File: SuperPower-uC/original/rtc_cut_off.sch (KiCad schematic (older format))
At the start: 8 parts, among them J601 Conn_01x02_Male, U601 RV-3028-C7

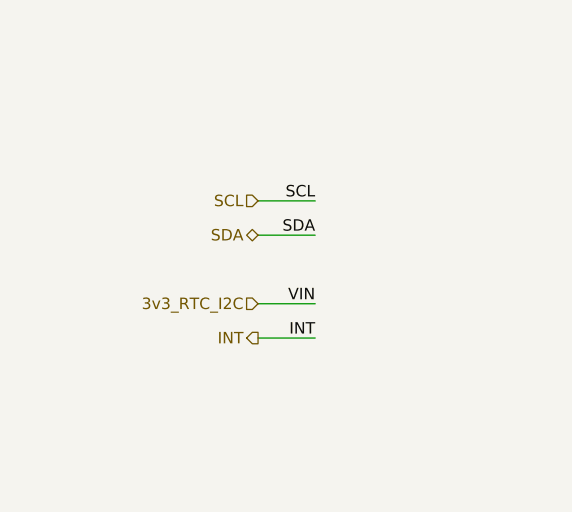
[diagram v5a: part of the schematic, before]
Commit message: Cleanup of text, boxes, label rotations etc. + add labels to main sheet for better overview
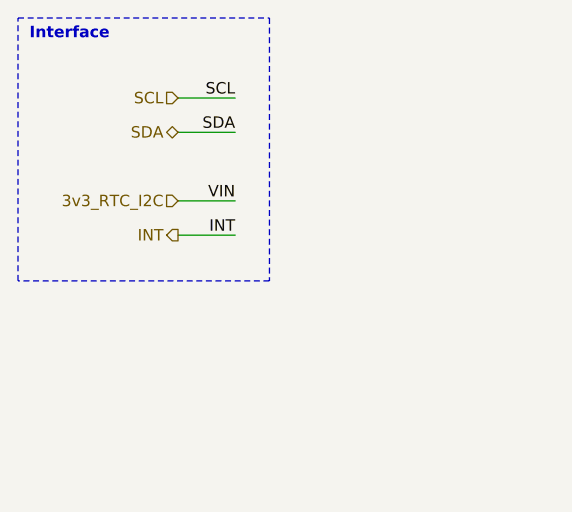
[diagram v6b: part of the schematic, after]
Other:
- note added: "Interface"
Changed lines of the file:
@@
 Comment4 ""
 $EndDescr
-Text HLabel 1600 1350 0    50   Input ~ 0
-SCL
-Text HLabel 1600 1500 0    50   BiDi ~ 0
-SDA
-Text HLabel 1600 1950 0    50   Output ~ 0
+Text HLabel 1250 900  0    50   Input ~ 0
+SCL
+Text HLabel 1250 1050 0    50   BiDi ~ 0
+SDA
+Text HLabel 1250 1500 0    50   Output ~ 0
 INT
 NoConn ~ 5900 3550
@@
 Text Label 4250 3650 0    50   ~ 0
 SDA
-Text Label 1850 1350 2    50   ~ 0
-SCL
-Text Label 1850 1500 2    50   ~ 0
-SDA
-Text Label 1850 1950 2    50   ~ 0
+Text Label 1500 900  2    50   ~ 0
+SCL
+Text Label 1500 1050 2    50   ~ 0
+SDA
+Text Label 1500 1500 2    50   ~ 0
 INT
 Wire Wire Line
-	1600 1950 1850 1950
-Wire Wire Line
-	1600 1350 1850 1350
-Wire Wire Line
-	1600 1500 1850 1500
+	1250 1500 1500 1500
+Wire Wire Line
+	1250 900  1500 900
+Wire Wire Line
+	1250 1050 1500 1050
 Wire Wire Line
 	4500 3550 4250 3550
@@
 Text Label 1650 3850 0    50   ~ 0
 SCL
-Text HLabel 1600 1800 0    50   Input ~ 0
+Text HLabel 1250 1350 0    50   Input ~ 0
 3v3_RTC_I2C
 Text Label 6850 2650 3    50   ~ 0
@@
 VIN
 Wire Wire Line
-	1600 1800 1850 1800
-Text Label 1850 1800 2    50   ~ 0
+	1250 1350 1500 1350
+Text Label 1500 1350 2    50   ~ 0
 VIN
 Wire Wire Line
@@
 Wire Wire Line
 	1650 3200 1650 3450
+Text Notes 600  650  0    50   ~ 10
+Interface
+Wire Notes Line
+	550  550  1650 550
+Wire Notes Line
+	1650 550  1650 1700
+Wire Notes Line
+	1650 1700 550  1700
+Wire Notes Line
+	550  1700 550  550
 $EndSCHEMATC

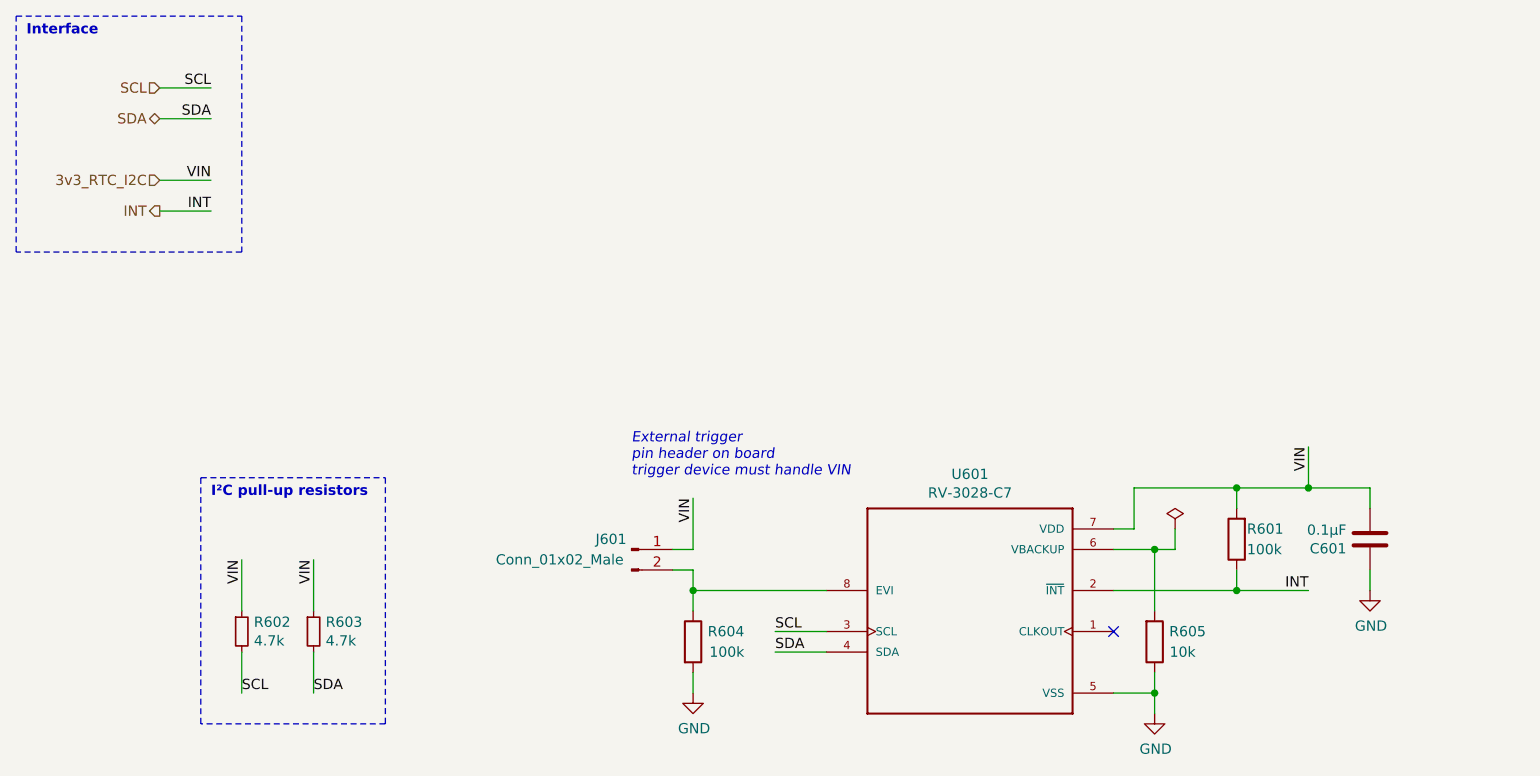
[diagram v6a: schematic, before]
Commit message: Update regulator symbol, changed MOSFET switching of regulators
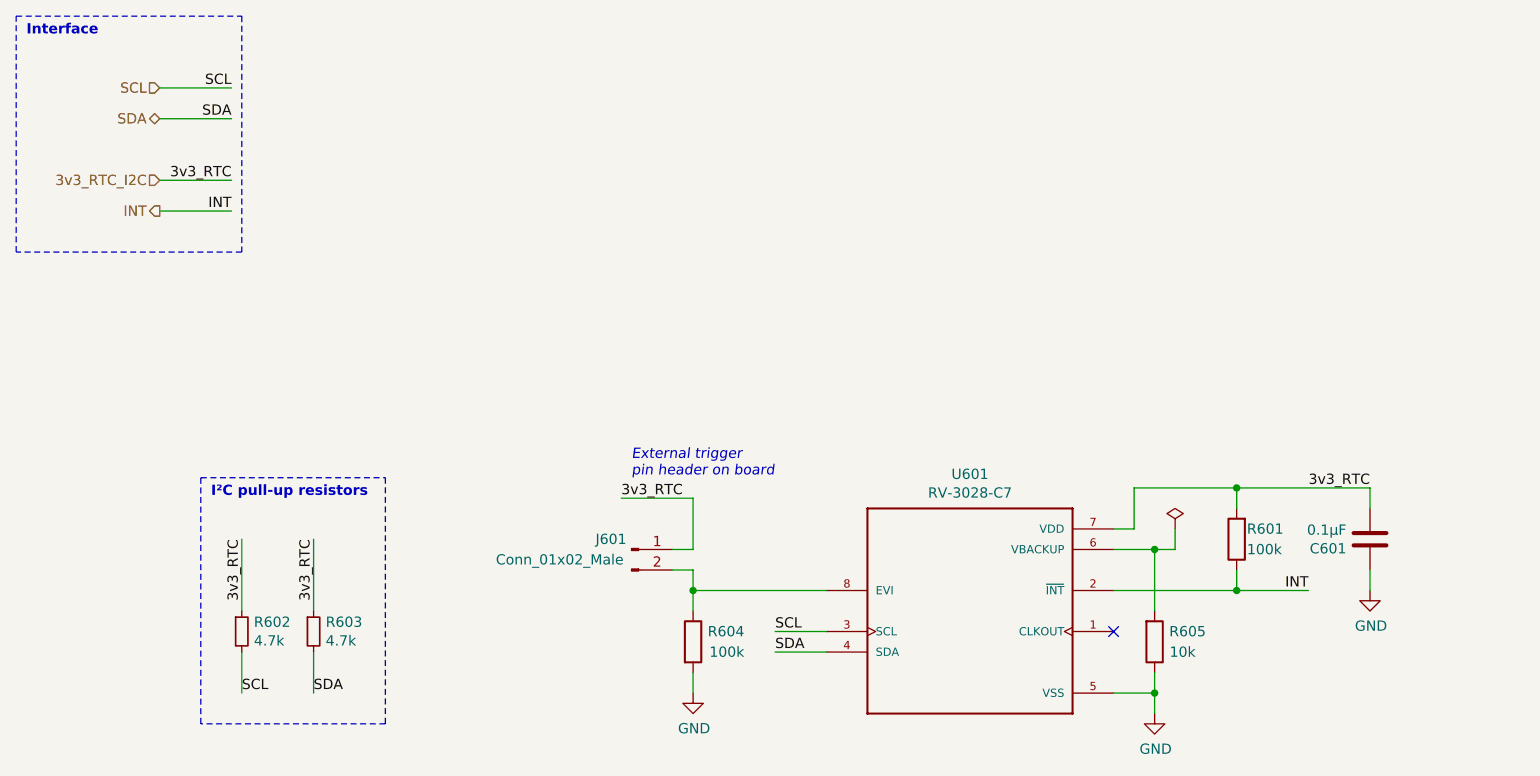
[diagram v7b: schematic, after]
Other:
- note added: "External trigger\npin header on board"
- note removed: "External trigger\npin header on board\ntrigger device must handle VIN"
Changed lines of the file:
@@
 Text Label 4250 3650 0    50   ~ 0
 SDA
-Text Label 1500 900  2    50   ~ 0
+Text Label 1600 900  2    50   ~ 0
 SCL
-Text Label 1500 1050 2    50   ~ 0
+Text Label 1600 1050 2    50   ~ 0
 SDA
-Text Label 1500 1500 2    50   ~ 0
+Text Label 1600 1500 2    50   ~ 0
 INT
 Wire Wire Line
-	1250 1500 1500 1500
-Wire Wire Line
-	1250 900  1500 900
-Wire Wire Line
-	1250 1050 1500 1050
+	1250 1500 1600 1500
+Wire Wire Line
+	1250 900  1600 900
+Wire Wire Line
+	1250 1050 1600 1050
 Wire Wire Line
 	4500 3550 4250 3550
@@
 Wire Wire Line
 	6500 3350 6850 3350
-Wire Wire Line
-	6850 2850 7150 2850
-Wire Wire Line
-	6500 2850 6850 2850
-Connection ~ 6850 2850
 $Comp
 L Device:R_Small R?
@@
 Text HLabel 1250 1350 0    50   Input ~ 0
 3v3_RTC_I2C
-Text Label 6850 2650 3    50   ~ 0
-VIN
-Wire Wire Line
-	6850 2650 6850 2850
+Text Label 7150 2850 2    50   ~ 0
+3v3_RTC
 Wire Wire Line
 	3850 2900 3850 3150
-Text Label 3850 2900 3    50   ~ 0
-VIN
+Text Label 3500 2900 0    50   ~ 0
+3v3_RTC
 Text Notes 3550 2800 0    50   Italic 0
-External trigger\npin header on board\ntrigger device must handle VIN
-Text Label 2000 3200 3    50   ~ 0
-VIN
-Text Label 1650 3200 3    50   ~ 0
-VIN
-Wire Wire Line
-	1250 1350 1500 1350
-Text Label 1500 1350 2    50   ~ 0
-VIN
-Wire Wire Line
-	2000 3200 2000 3450
-Wire Wire Line
-	1650 3200 1650 3450
+External trigger\npin header on board
+Text Label 2000 3100 3    50   ~ 0
+3v3_RTC
+Text Label 1650 3100 3    50   ~ 0
+3v3_RTC
+Wire Wire Line
+	1250 1350 1600 1350
+Text Label 1600 1350 2    50   ~ 0
+3v3_RTC
+Wire Wire Line
+	2000 3100 2000 3450
+Wire Wire Line
+	1650 3100 1650 3450
 Text Notes 600  650  0    50   ~ 10
 Interface
@@
 Wire Notes Line
 	550  1700 550  550
+Wire Wire Line
+	3500 2900 3850 2900
+Wire Wire Line
+	6500 2850 7150 2850
 $EndSCHEMATC

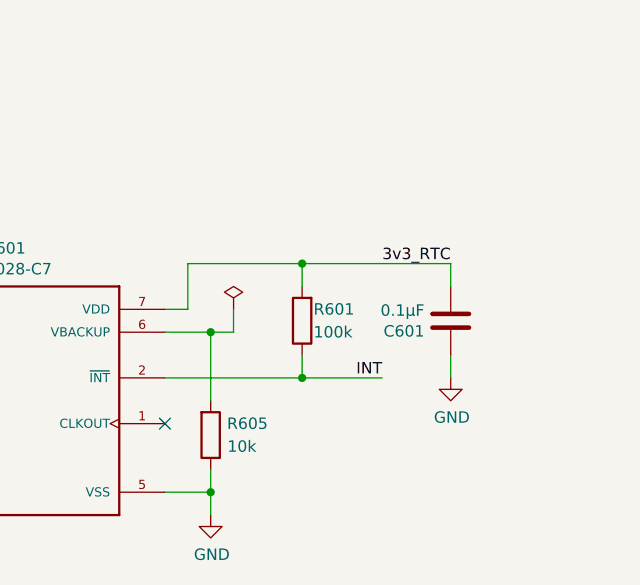
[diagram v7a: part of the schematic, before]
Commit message: Update Regulator and RTC sheets
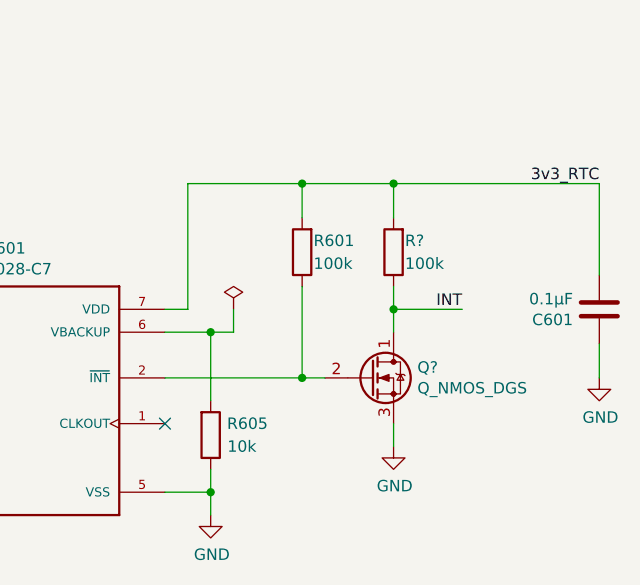
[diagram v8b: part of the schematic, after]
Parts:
- added Q?: Q_NMOS_DGS, symbol Device:Q_NMOS_DGS
- added R?: 100k, Resistors_SMD:R_0603, symbol Device:R
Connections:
- net 3v3_RTC_I2C: now also R?.2
- net GND: now also Q?.3 (S)
- net INT: now also Q?.1 (D), R?.1; no longer R601.1, U601.2 (~INT~)
- new net: Q?.2 (G), R601.1, U601.2 (~INT~)
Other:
- moved on the sheet: C601, R601
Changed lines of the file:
@@
 L Device:R R601
 U 1 1 5F716136
-P 6500 3100
-F 0 "R601" H 6450 3050 50  0000 R CNN
-F 1 "100k" H 6450 3150 50  0000 R CNN
-F 2 "Resistors_SMD:R_0603" V 6430 3100 50  0001 C CNN
-F 3 "~" H 6500 3100 50  0001 C CNN
-	1    6500 3100
+P 6500 2800
+F 0 "R601" H 6450 2750 50  0000 R CNN
+F 1 "100k" H 6450 2850 50  0000 R CNN
+F 2 "Resistors_SMD:R_0603" V 6430 2800 50  0001 C CNN
+F 3 "~" H 6500 2800 50  0001 C CNN
+	1    6500 2800
 	-1   0    0    1
 $EndComp
@@
 L Device:C C601
 U 1 1 5F716113
-P 7150 3100
-F 0 "C601" H 7265 3146 50  0000 L CNN
-F 1 "0.1µF" H 7265 3055 50  0000 L CNN
-F 2 "Capacitors_SMD:C_0603" H 7188 2950 50  0001 C CNN
-F 3 "~" H 7150 3100 50  0001 C CNN
-	1    7150 3100
+P 7800 3050
+F 0 "C601" H 7915 3096 50  0000 L CNN
+F 1 "0.1µF" H 7915 3005 50  0000 L CNN
+F 2 "Capacitors_SMD:C_0603" H 7838 2900 50  0001 C CNN
+F 3 "~" H 7800 3050 50  0001 C CNN
+	1    7800 3050
 	-1   0    0    1
 $EndComp
 Wire Wire Line
-	7150 2950 7150 2850
-Text Label 6850 3350 2    50   ~ 0
+	7800 2900 7800 2500
+Text Label 7200 3050 2    50   ~ 0
 INT
 $Comp
@@
 L power:GND #PWR0601
 U 1 1 5FBD2731
-P 7150 3350
-F 0 "#PWR0601" H 7150 3100 50  0001 C CNN
-F 1 "GND" H 7155 3177 50  0000 C CNN
-F 2 "" H 7150 3350 50  0001 C CNN
-F 3 "" H 7150 3350 50  0001 C CNN
-	1    7150 3350
-	1    0    0    -1
-$EndComp
-Wire Wire Line
-	7150 3250 7150 3350
+P 7800 3350
+F 0 "#PWR0601" H 7800 3100 50  0001 C CNN
+F 1 "GND" H 7805 3177 50  0000 C CNN
+F 2 "" H 7800 3350 50  0001 C CNN
+F 3 "" H 7800 3350 50  0001 C CNN
+	1    7800 3350
+	1    0    0    -1
+$EndComp
+Wire Wire Line
+	7800 3200 7800 3350
 Wire Wire Line
 	5900 3350 6500 3350
 Wire Wire Line
-	6500 3250 6500 3350
-Wire Wire Line
-	6500 2850 6500 2950
+	6500 2950 6500 3350
+Wire Wire Line
+	6500 2500 6500 2650
 Wire Wire Line
 	6000 3050 5900 3050
 Wire Wire Line
-	6000 3050 6000 2850
-Wire Wire Line
-	6000 2850 6500 2850
-Connection ~ 6500 2850
+	6000 3050 6000 2500
+Wire Wire Line
+	6000 2500 6500 2500
+Connection ~ 6500 2500
 Connection ~ 6500 3350
 Wire Wire Line
-	6500 3350 6850 3350
+	6500 3350 6600 3350
 $Comp
 L Device:R_Small R?
@@
 Text HLabel 1250 1350 0    50   Input ~ 0
 3v3_RTC_I2C
-Text Label 7150 2850 2    50   ~ 0
+Text Label 7800 2500 2    50   ~ 0
 3v3_RTC
 Wire Wire Line
@@
 	3500 2900 3850 2900
 Wire Wire Line
-	6500 2850 7150 2850
+	6500 2500 6900 2500
+$Comp
+L Device:Q_NMOS_DGS Q?
+U 1 1 5FCB2D78
+P 6800 3350
+F 0 "Q?" H 7004 3396 50  0000 L CNN
+F 1 "Q_NMOS_DGS" H 7004 3305 50  0000 L CNN
+F 2 "" H 7000 3450 50  0001 C CNN
+F 3 "~" H 6800 3350 50  0001 C CNN
+	1    6800 3350
+	1    0    0    -1
+$EndComp
+$Comp
+L power:GND #PWR?
+U 1 1 5FCB73B1
+P 6900 3650
+F 0 "#PWR?" H 6900 3400 50  0001 C CNN
+F 1 "GND" H 6905 3477 50  0000 C CNN
+F 2 "" H 6900 3650 50  0001 C CNN
+F 3 "" H 6900 3650 50  0001 C CNN
+	1    6900 3650
+	1    0    0    -1
+$EndComp
+Wire Wire Line
+	6900 3550 6900 3650
+Wire Wire Line
+	6900 3150 6900 3050
+Wire Wire Line
+	6900 3050 7200 3050
+$Comp
+L Device:R R?
+U 1 1 5FCCE813
+P 6900 2800
+F 0 "R?" H 6850 2750 50  0000 R CNN
+F 1 "100k" H 6850 2850 50  0000 R CNN
+F 2 "Resistors_SMD:R_0603" V 6830 2800 50  0001 C CNN
+F 3 "~" H 6900 2800 50  0001 C CNN
+	1    6900 2800
+	-1   0    0    1
+$EndComp
+Wire Wire Line
+	6900 2950 6900 3050
+Connection ~ 6900 3050
+Wire Wire Line
+	6900 2650 6900 2500
+Connection ~ 6900 2500
+Wire Wire Line
+	6900 2500 7800 2500
 $EndSCHEMATC
